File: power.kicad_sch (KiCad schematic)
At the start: 39 parts, among them J1 Battery 1, J7 Battery 2, J8 USB, U1 AMS1117-3.3, U5 TPS62933, U6 TPS62933

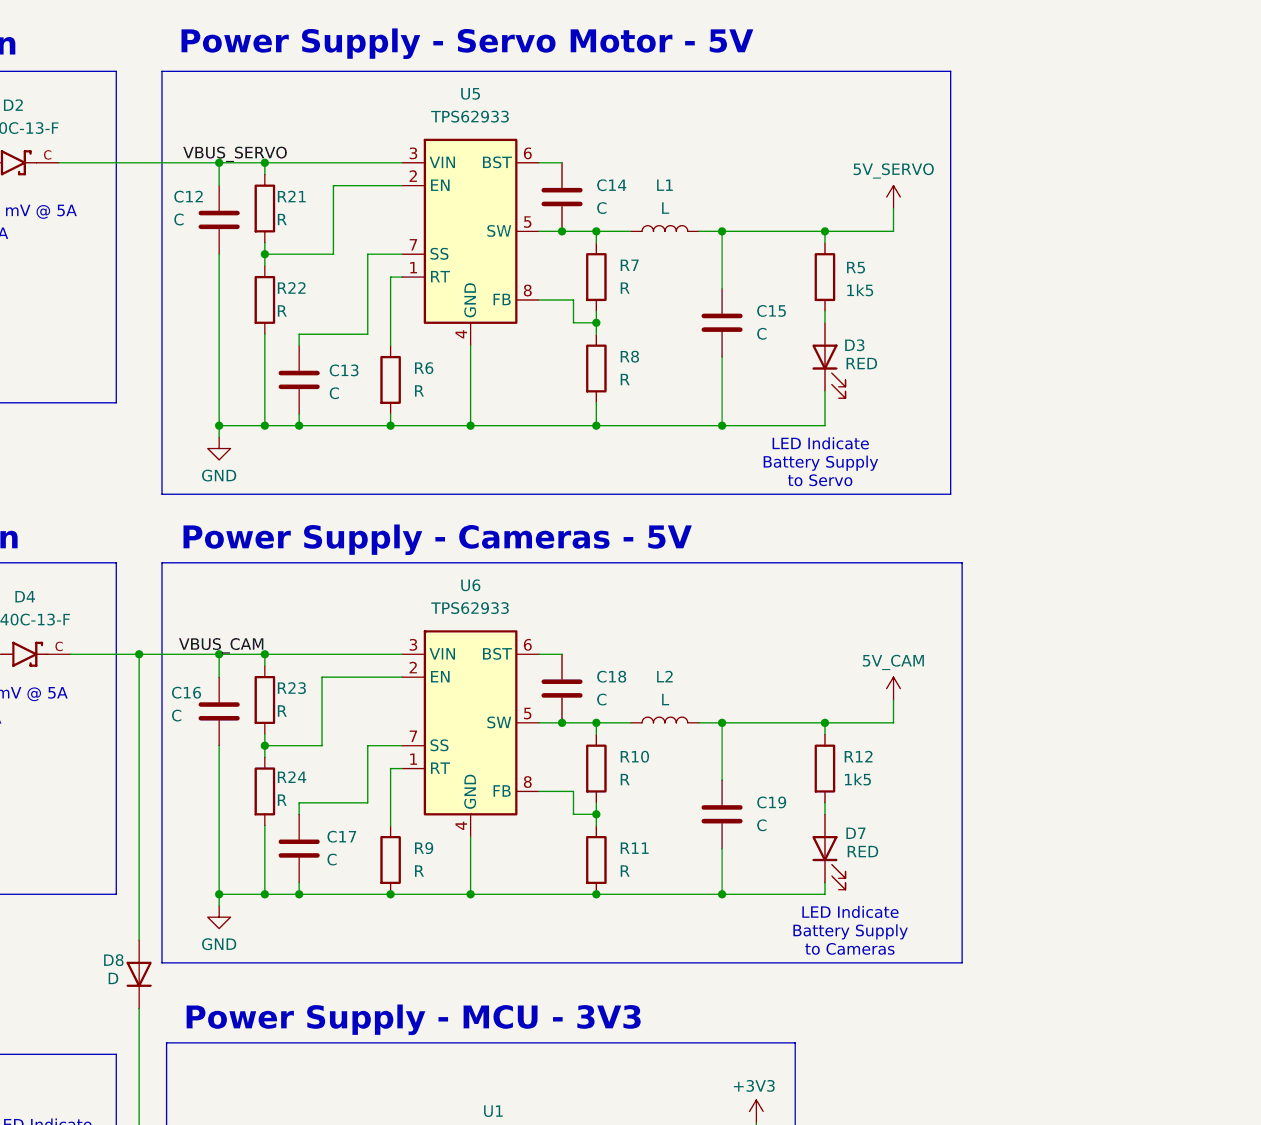
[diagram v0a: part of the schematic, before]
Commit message: Remove transistor enable for servo power. Added falstad sim files
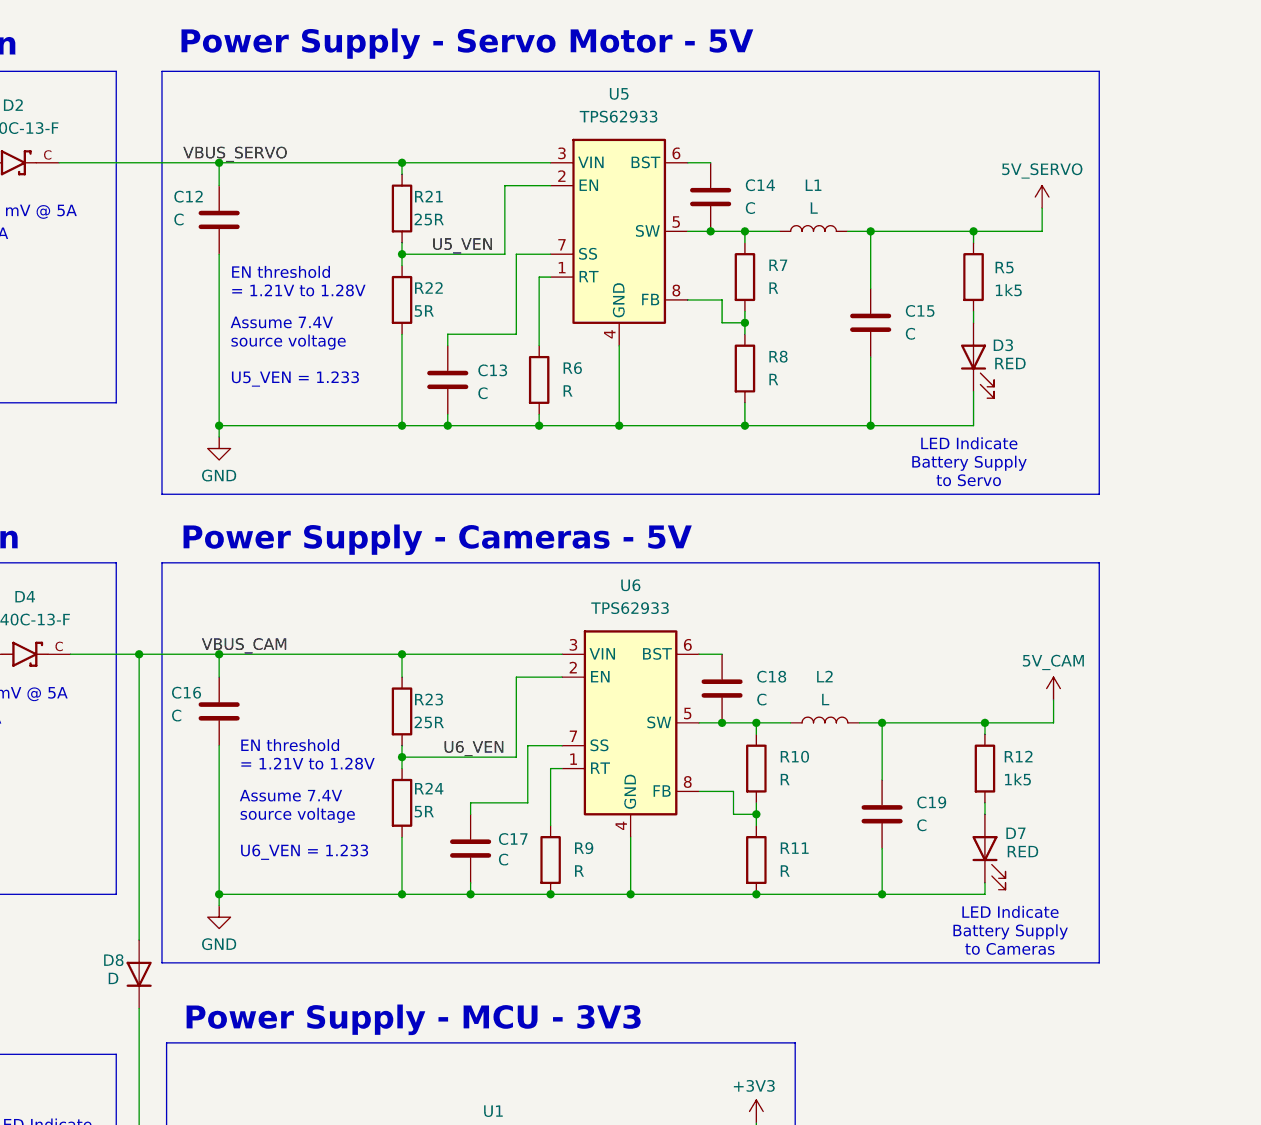
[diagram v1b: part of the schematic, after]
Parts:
- R21, R23: value R -> 25R
- R22, R24: value R -> 5R
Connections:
- net U6_VEN: now reaches R23.2, R24.1, U6.2 (EN)
- net U5_VEN: now reaches R21.2, R22.1, U5.2 (EN)
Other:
- note added: "Assume 7.4V source voltage"
- note added: "EN threshold = 1.21V to 1.28V"
- note added: "U5_VEN = 1.233"
- note added: "U6_VEN = 1.233"
- moved on the sheet: C13, C14, C15, C17, C18, C19, D3, D7, L1, L2, R10, R11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

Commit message: Updated schematics
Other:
- note added: "CAS Board 2025"
- note removed: "Simpler Flight v2"

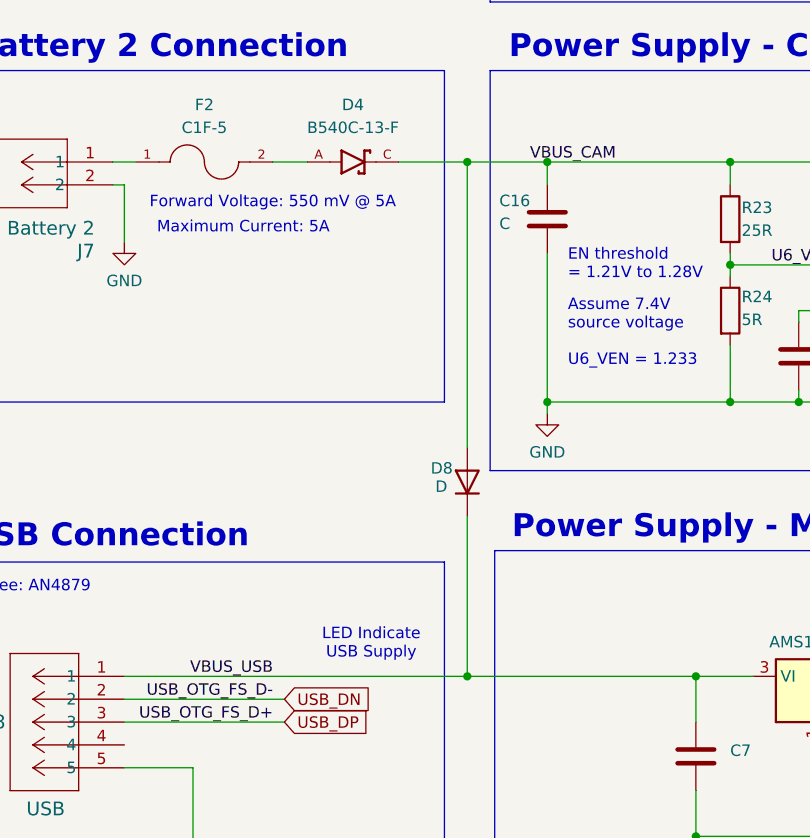
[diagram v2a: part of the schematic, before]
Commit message: use another shotkey diode for battery to usb intersection for mcu power
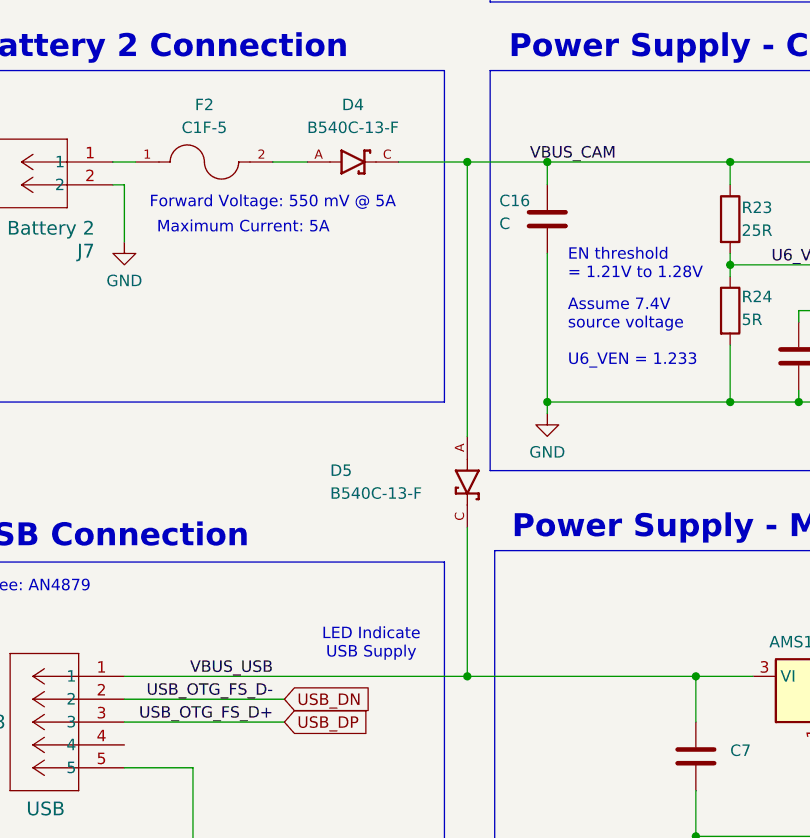
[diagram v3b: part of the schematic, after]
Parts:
- removed D8: D, Diode_SMD:D_0805_2012Metric_Pad1.15x1.40mm_HandSolder, symbol Device:D
- added D5: B540C-13-F, B540C_13_F:DIOM6959X245N, symbol B540C-13-F:B540C-13-F
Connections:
- net VBUS_CAM: now also D5.A
- net VBUS_USB: now also D5.C
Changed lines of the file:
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@@
 	)
 	(junction
+		(at 73.66 143.51)
+		(diameter 0)
+		(color 0 0 0 0)
+	)
+	(junction
 		(at 134.62 143.51)
 		(diameter 0)
@@
 	)
 	(junction
-		(at 123.19 161.29)
-		(diameter 0)
-		(color 0 0 0 0)
-	)
-	(junction
 		(at 73.66 86.36)
 		(diameter 0)
@@
 	)
 	(junction
-		(at 82.55 86.36)
+		(at 123.19 161.29)
 		(diameter 0)
 		(color 0 0 0 0)
 	)
 	(junction
-		(at 73.66 143.51)
+		(at 82.55 86.36)
 		(diameter 0)
 		(color 0 0 0 0)
@@
 	(wire
 		(pts
+			(xy 73.66 86.36) (xy 73.66 116.84)
+		)
+		(stroke
+			(width 0)
+			(type default)
+		)
+	)
+	(wire
+		(pts
 			(xy 34.29 31.75) (xy 36.83 31.75)
 		)
@@
 	(wire
 		(pts
-			(xy 115.57 50.8) (xy 107.95 50.8)
+			(xy 73.66 127) (xy 73.66 143.51)
 		)
 		(stroke
@@
 	(wire
 		(pts
-			(xy 73.66 143.51) (xy 99.06 143.51)
+			(xy 115.57 50.8) (xy 107.95 50.8)
 		)
 		(stroke
@@
 	(wire
 		(pts
-			(xy 102.87 97.79) (xy 102.87 99.06)
+			(xy 35.56 143.51) (xy 73.66 143.51)
 		)
 		(stroke
@@
 	(wire
 		(pts
-			(xy 73.66 86.36) (xy 73.66 118.11)
+			(xy 102.87 97.79) (xy 102.87 99.06)
 		)
 		(stroke
@@
 	(wire
 		(pts
+			(xy 73.66 143.51) (xy 99.06 143.51)
+		)
+		(stroke
+			(width 0)
+			(type default)
+		)
+	)
+	(wire
+		(pts
 			(xy 156.21 93.98) (xy 167.64 93.98)
 		)
@@
 	(wire
 		(pts
-			(xy 142.24 143.51) (xy 134.62 143.51)
+			(xy 73.66 86.36) (xy 82.55 86.36)
 		)
 		(stroke
@@
 	(wire
 		(pts
-			(xy 110.49 111.76) (xy 110.49 113.03)
+			(xy 142.24 143.51) (xy 134.62 143.51)
 		)
 		(stroke
@@
 	(wire
 		(pts
-			(xy 135.89 101.6) (xy 139.7 101.6)
+			(xy 110.49 111.76) (xy 110.49 113.03)
 		)
 		(stroke
@@
 	(wire
 		(pts
-			(xy 110.49 113.03) (xy 119.38 113.03)
+			(xy 135.89 101.6) (xy 139.7 101.6)
 		)
 		(stroke
@@
 	(wire
 		(pts
-			(xy 99.06 161.29) (xy 113.03 161.29)
+			(xy 110.49 113.03) (xy 119.38 113.03)
 		)
 		(stroke
@@
 	(wire
 		(pts
-			(xy 35.56 143.51) (xy 73.66 143.51)
+			(xy 99.06 161.29) (xy 113.03 161.29)
 		)
 		(stroke
@@
 	(wire
 		(pts
-			(xy 66.04 86.36) (xy 73.66 86.36)
-		)
-		(stroke
-			(width 0)
-			(type default)
-		)
-	)
-	(wire
-		(pts
 			(xy 82.55 88.9) (xy 82.55 86.36)
 		)
@@
 	(wire
 		(pts
-			(xy 73.66 125.73) (xy 73.66 143.51)
-		)
-		(stroke
-			(width 0)
-			(type default)
-		)
-	)
-	(wire
-		(pts
 			(xy 34.29 34.29) (xy 35.56 34.29)
 		)
@@
 	(wire
 		(pts
-			(xy 73.66 86.36) (xy 82.55 86.36)
+			(xy 66.04 86.36) (xy 73.66 86.36)
 		)
 		(stroke
@@
 	)
 	(symbol
+		(lib_id "B540C-13-F:B540C-13-F")
+		(at 73.66 121.92 270)
+		(unit 1)
+		(exclude_from_sim no)
+		(in_bom yes)
+		(on_board yes)
+		(dnp no)
+		(property "Reference" "D5"
+			(at 58.42 120.65 90)
+			(effects
+				(font
+					(size 1.27 1.27)
+				)
+				(justify left)
+			)
+		)
+		(property "Value" "B540C-13-F"
+			(at 58.42 123.19 90)
+			(effects
+				(font
+					(size 1.27 1.27)
+				)
+				(justify left)
+			)
+		)
+		(property "Footprint" "B540C_13_F:DIOM6959X245N"
+			(at 73.66 121.92 0)
+			(effects
+				(font
+					(size 1.27 1.27)
+				)
+				(justify bottom)
+				(hide yes)
+			)
+		)
+		(property "Datasheet" ""
+			(at 73.66 121.92 0)
+			(effects
+				(font
+					(size 1.27 1.27)
+				)
+				(hide yes)
+			)
+		)
+		(property "Description" ""
+			(at 73.66 121.92 0)
+			(effects
+				(font
+					(size 1.27 1.27)
+				)
+				(hide yes)
+			)
+		)
+		(property "PARTREV" "V1.0"
+			(at 73.66 121.92 0)
+			(effects
+				(font
+					(size 1.27 1.27)
+				)
+				(justify bottom)
+				(hide yes)
+			)
+		)
+		(property "STANDARD" "IPC 7351B"
+			(at 73.66 121.92 0)
+			(effects
+				(font
+					(size 1.27 1.27)
+				)
+				(justify bottom)
+				(hide yes)
+			)
+		)
+		(property "MAXIMUM_PACKAGE_HEIGHT" "2.45 mm"
+			(at 73.66 121.92 0)
+			(effects
+				(font
+					(size 1.27 1.27)
+				)
+				(justify bottom)
+				(hide yes)
+			)
+		)
+		(property "MANUFACTURER" "multicomp"
+			(at 73.66 121.92 0)
+			(effects
+				(font
+					(size 1.27 1.27)
+				)
+				(justify bottom)
+				(hide yes)
+			)
+		)
+		(pin "C"
+		)
+		(pin "A"
+		)
+		(instances
+			(project "SimplerFlight_v2"
+				(path "/05521696-5bcb-4d0e-9e87-bbc993e58ce4/9c9f06bc-de18-4b20-a7a6-016e96dea1cf"
+					(reference "D5")
+					(unit 1)
+				)
+			)
+		)
+	)
+	(symbol
 		(lib_id "Device:C")
 		(at 154.94 49.53 0)
@@
 					(unit 1)
 				)
-			)
-		)
-	)
-	(symbol
-		(lib_id "Device:D")
-		(at 73.66 121.92 90)
-		(unit 1)
-		(exclude_from_sim no)
-		(in_bom yes)
-		(on_board yes)
-		(dnp no)
-		(property "Reference" "D8"
-			(at 69.596 120.396 90)
-			(effects
-				(font
-					(size 1.27 1.27)
-				)
-				(justify right)
-			)
-		)
-		(property "Value" "D"
-			(at 70.104 122.428 90)
-			(effects
-				(font
-					(size 1.27 1.27)
-				)
-				(justify right)
-			)
-		)
-		(property "Footprint" "Diode_SMD:D_0805_2012Metric_Pad1.15x1.40mm_HandSolder"
-			(at 73.66 121.92 0)
-			(effects
-				(font
-					(size 1.27 1.27)
-				)
-				(hide yes)
-			)
-		)
-		(property "Datasheet" "~"
-			(at 73.66 121.92 0)
-			(effects
-				(font
-					(size 1.27 1.27)
-				)
-				(hide yes)
-			)
-		)
-		(property "Description" "Diode"
-			(at 73.66 121.92 0)
-			(effects
-				(font
-					(size 1.27 1.27)
-				)
-				(hide yes)
-			)
-		)
-		(property "Sim.Device" "D"
-			(at 73.66 121.92 0)
-			(effects
-				(font
-					(size 1.27 1.27)
-				)
-				(hide yes)
-			)
-		)
-		(property "Sim.Pins" "1=K 2=A"
-			(at 73.66 121.92 0)
-			(effects
-				(font
-					(size 1.27 1.27)
-				)
-				(hide yes)
-			)
-		)
-		(pin "1"
-		)
-		(pin "2"
-		)
-		(instances
-			(project "SimplerFlight_v2"
-				(path "/05521696-5bcb-4d0e-9e87-bbc993e58ce4/9c9f06bc-de18-4b20-a7a6-016e96dea1cf"
-					(reference "D8")
-					(unit 1)
-				)
